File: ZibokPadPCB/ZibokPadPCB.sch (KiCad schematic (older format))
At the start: 68 parts, among them Q1 DTC123J, SW1 Rotary_Encoder_Switch, U1 STM32F072C8Tx, U2 USBLC6-2SC6, U3 MCP1700-3302E_SOT23

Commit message: routing
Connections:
- net D+: now also U2.1 (IO1); no longer U2.3 (IO2)
- net D-: now also U2.3 (IO2); no longer U2.1 (IO1)
- net DBus+: now also U2.6 (IO1); no longer U2.4 (IO2)
- net Dbus-: now also U2.4 (IO2); no longer U2.6 (IO1)
- net GND: now also CRST2.1
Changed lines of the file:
@@
 Text GLabel 4150 2050 1    50   Input ~ 0
 VBUS
+Text GLabel 3650 2700 0    50   Input ~ 0
+DBus+
 Text GLabel 4650 2700 2    50   Input ~ 0
-DBus+
-Text GLabel 3650 2700 0    50   Input ~ 0
 Dbus-
+Text GLabel 4650 2900 2    50   Input ~ 0
+D-
 Text GLabel 3650 2900 0    50   Input ~ 0
-D-
-Text GLabel 4650 2900 2    50   Input ~ 0
 D+
 $Comp
@@
 Text GLabel 11050 2050 0    50   Input ~ 0
 ROT2
+Wire Wire Line
+	950  600  1150 600
 $EndSCHEMATC

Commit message: Routing
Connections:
- net COL0: now also U1.22 (PB11)
- net COL1: now also U1.21 (PB10)
- net COL2: now also U1.20 (PB2)
- net COL3: now also U1.19 (PB1)
- net ROW0: now also U1.43 (PB7)
- net ROW1: now also U1.42 (PB6)
- net ROW2: now also U1.41 (PB5)
- net ROW3: now also U1.40 (PB4)
- net ROW4: now also U1.39 (PB3)
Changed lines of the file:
@@
 Wire Wire Line
 	950  600  1150 600
+Text GLabel 1350 5100 0    50   Input ~ 0
+ROW0
+Text GLabel 1350 5000 0    50   Input ~ 0
+ROW1
+Text GLabel 1350 4900 0    50   Input ~ 0
+ROW2
+Text GLabel 1350 4800 0    50   Input ~ 0
+ROW3
+Text GLabel 1350 4700 0    50   Input ~ 0
+ROW4
+Text GLabel 1350 5500 0    50   Input ~ 0
+COL0
+Text GLabel 1350 5400 0    50   Input ~ 0
+COL1
+Text GLabel 1350 4600 0    50   Input ~ 0
+COL2
+Text GLabel 1350 4500 0    50   Input ~ 0
+COL3
 $EndSCHEMATC

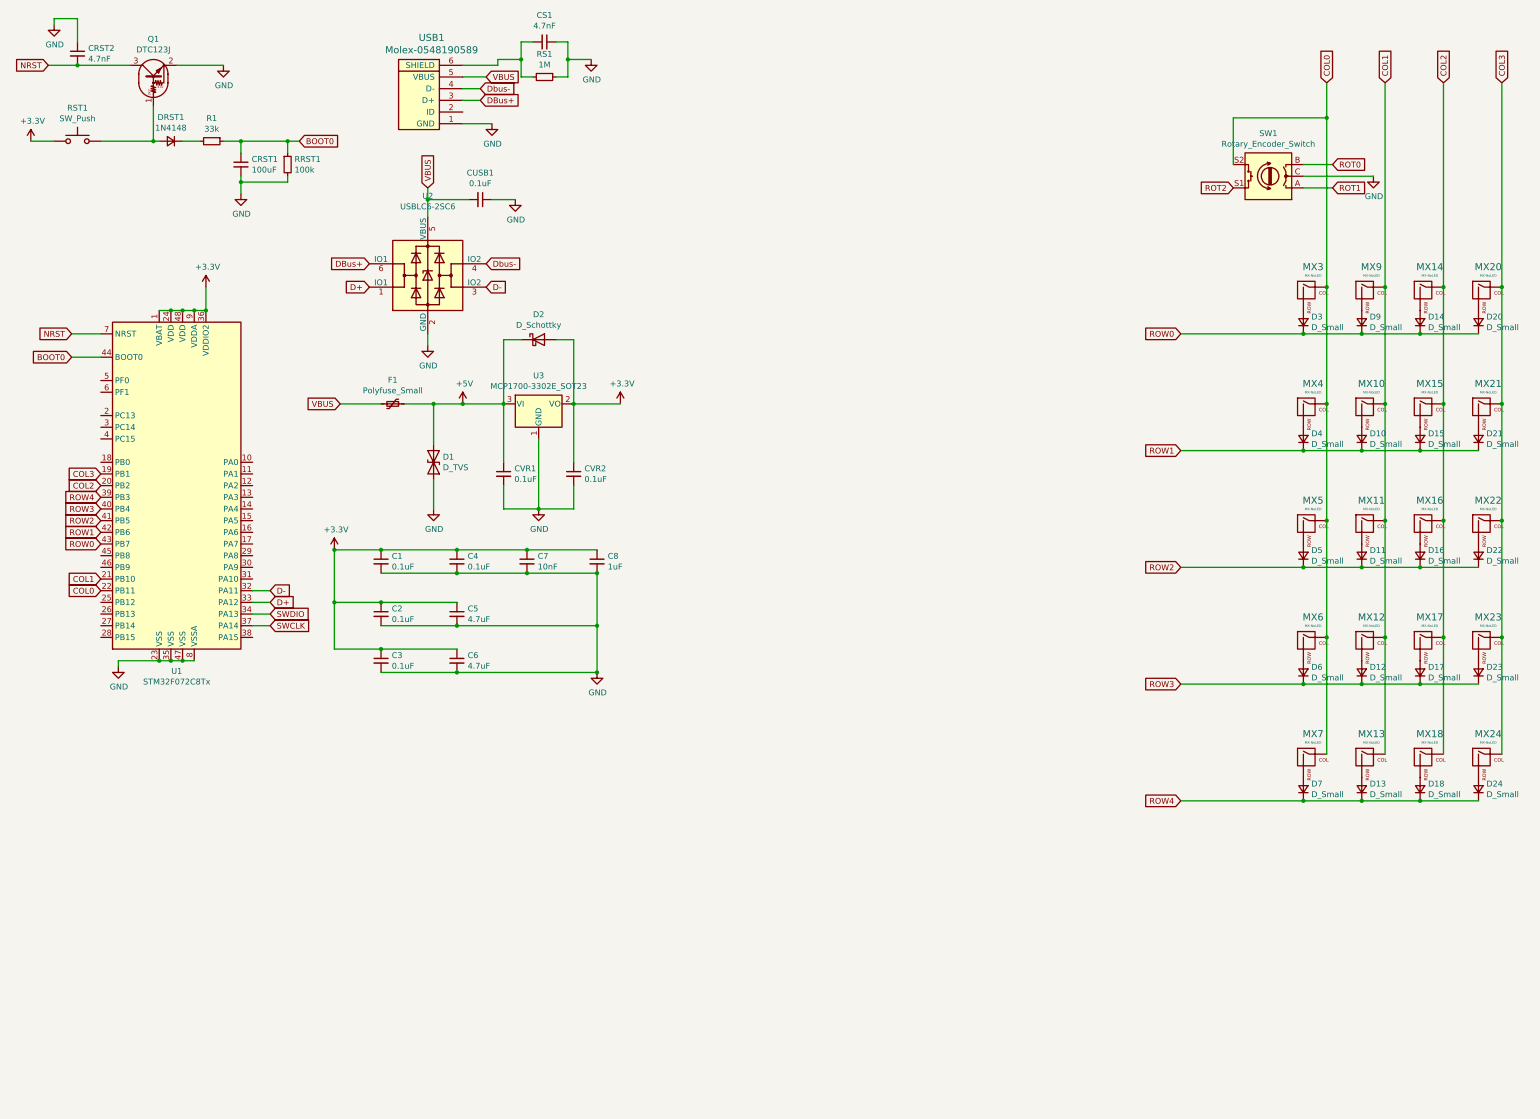
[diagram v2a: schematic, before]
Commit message: led work start
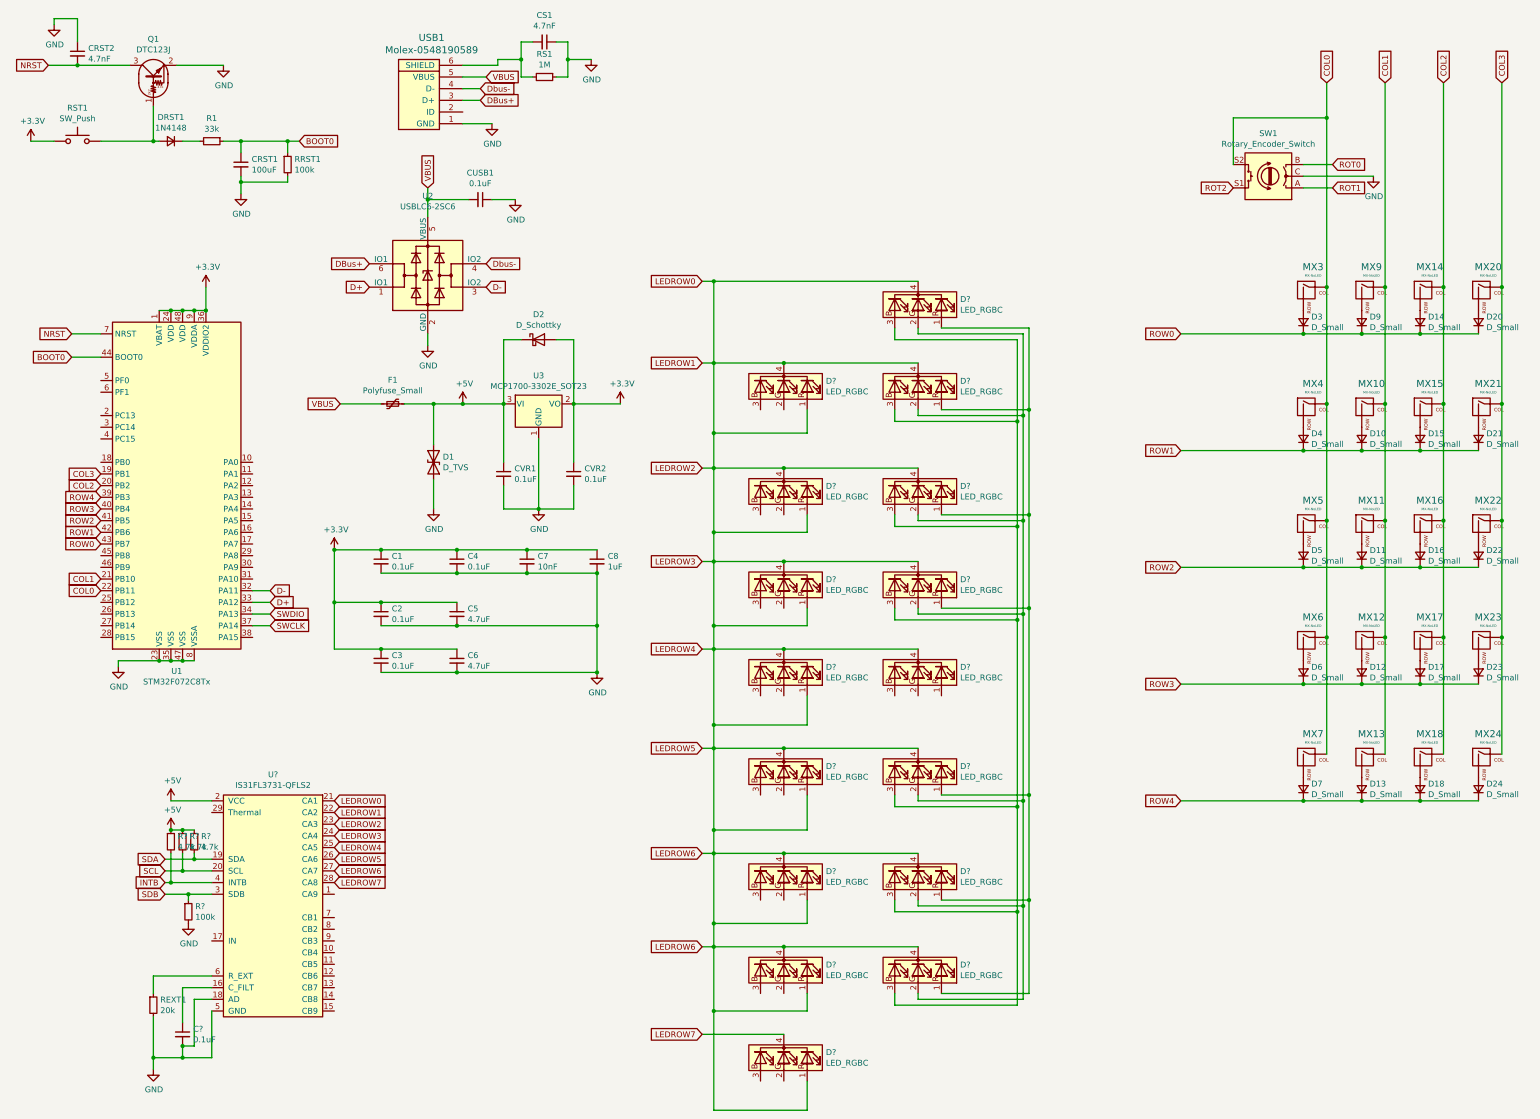
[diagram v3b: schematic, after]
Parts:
- added C?: 0.1uF, symbol Device:C_Small
- added D? (x16): LED_RGBC, symbol Device:LED_RGBC
- added R?: 100k, symbol Device:R_Small
- added R? (x3): 4.7k, symbol Device:R_Small
- added REXT1: 20k, symbol Device:R_Small
- added U?: IS31FL3731-QFLS2, symbol random-keyboard-parts:IS31FL3731-QFLS2
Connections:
- net +5V: now also R?.1, R?.1, R?.1, U?.2 (VCC)
- net GND: now also C?.2, R?.2, REXT1.2, U?.18 (AD), U?.5 (GND)
- new net: C?.1, U?.16 (C_FILT)
- new net: REXT1.1, U?.6 (R_EXT)
- new net: D?.1 (RA), D?.1 (RA), D?.1 (RA), D?.1 (RA), D?.1 (RA), D?.1 (RA), D?.1 (RA)
- new net: D?.2 (GA), D?.2 (GA), D?.2 (GA), D?.2 (GA), D?.2 (GA), D?.2 (GA), D?.2 (GA)
- new net: D?.3 (BA), D?.3 (BA), D?.3 (BA), D?.3 (BA), D?.3 (BA), D?.3 (BA), D?.3 (BA)
- new net INTB: R?.2, U?.4 (INTB)
- new net LEDROW0: D?.1 (RA), D?.1 (RA), D?.1 (RA), D?.1 (RA), D?.1 (RA), D?.1 (RA), D?.1 (RA), D?.1 (RA), D?.4 (K), D?.4 (K), D?.4 (K), D?.4 (K), D?.4 (K), D?.4 (K), D?.4 (K), D?.4 (K), D?.4 (K), D?.4 (K), D?.4 (K), D?.4 (K), D?.4 (K), D?.4 (K), D?.4 (K), U?.21 (CA1), U?.22 (CA2), U?.23 (CA3), U?.24 (CA4), U?.25 (CA5), U?.26 (CA6), U?.27 (CA7)
- new net LEDROW7: D?.4 (K), U?.28 (CA8)
- new net SCL: R?.2, U?.20 (SCL)
- new net SDA: R?.2, U?.19 (SDA)
- new net SDB: R?.1, U?.3 (SDB)
